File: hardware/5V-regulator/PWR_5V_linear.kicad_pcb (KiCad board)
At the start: 2 copper layers, 19.7 x 19.7 mm, 16 parts, among them P1002 CONN_1, P901 CONN_1, P902 CONN_1, Q1001 MOS_PRO, U1001 LM317M

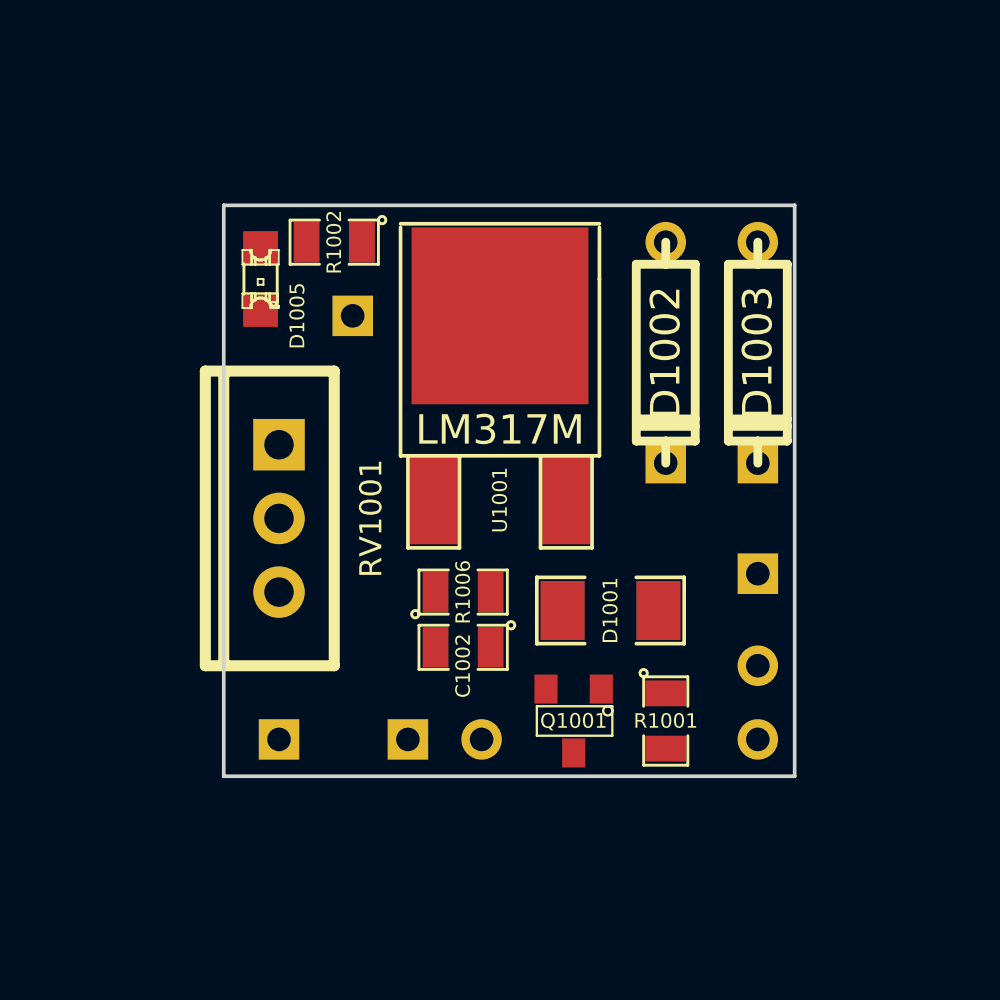
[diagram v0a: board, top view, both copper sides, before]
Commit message: 
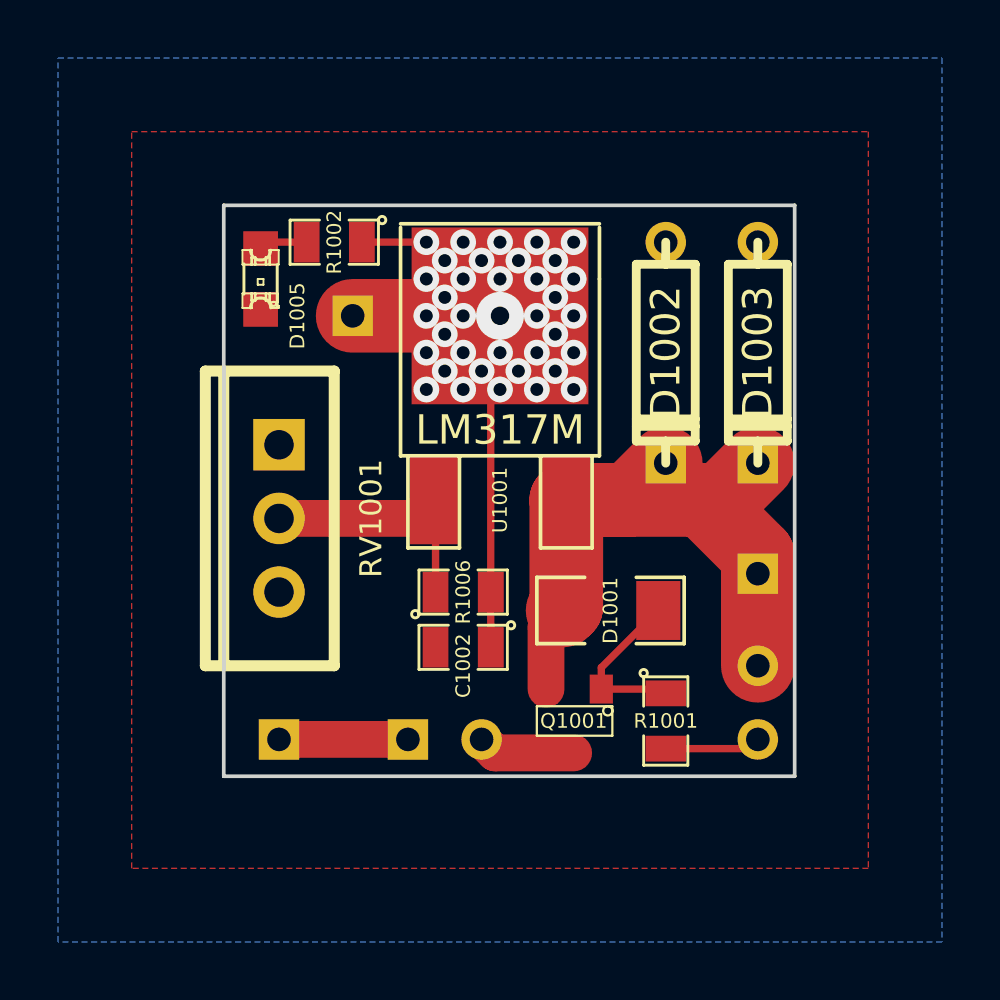
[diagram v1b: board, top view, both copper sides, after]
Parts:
- turned C1001 to 270 degrees
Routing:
- net /5V-REG: track 0.00 -> 62.4 mm, vias 0 -> 37
- net /VBAT: track 0.00 -> 24.4 mm
- net N-000003: track 0.00 -> 8.80 mm
- net N-000007: track 0.00 -> 5.81 mm
- net /Vin: track 0.00 -> 4.44 mm
- net /Vf: track 0.00 -> 3.37 mm
- net GND: track 0.00 -> 3.31 mm
- net N-000005: track 0.00 -> 1.68 mm
- added copper zone on B.Cu, net GND
- added copper zone on F.Cu, net GND
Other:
- net class .05 added: clearance 0.254, trace_width 1.27, via_dia 0.889, via_drill 0.635
- net class .1 added: clearance 0.254, trace_width 2.54, via_dia 1.651, via_drill 1.397

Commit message: 
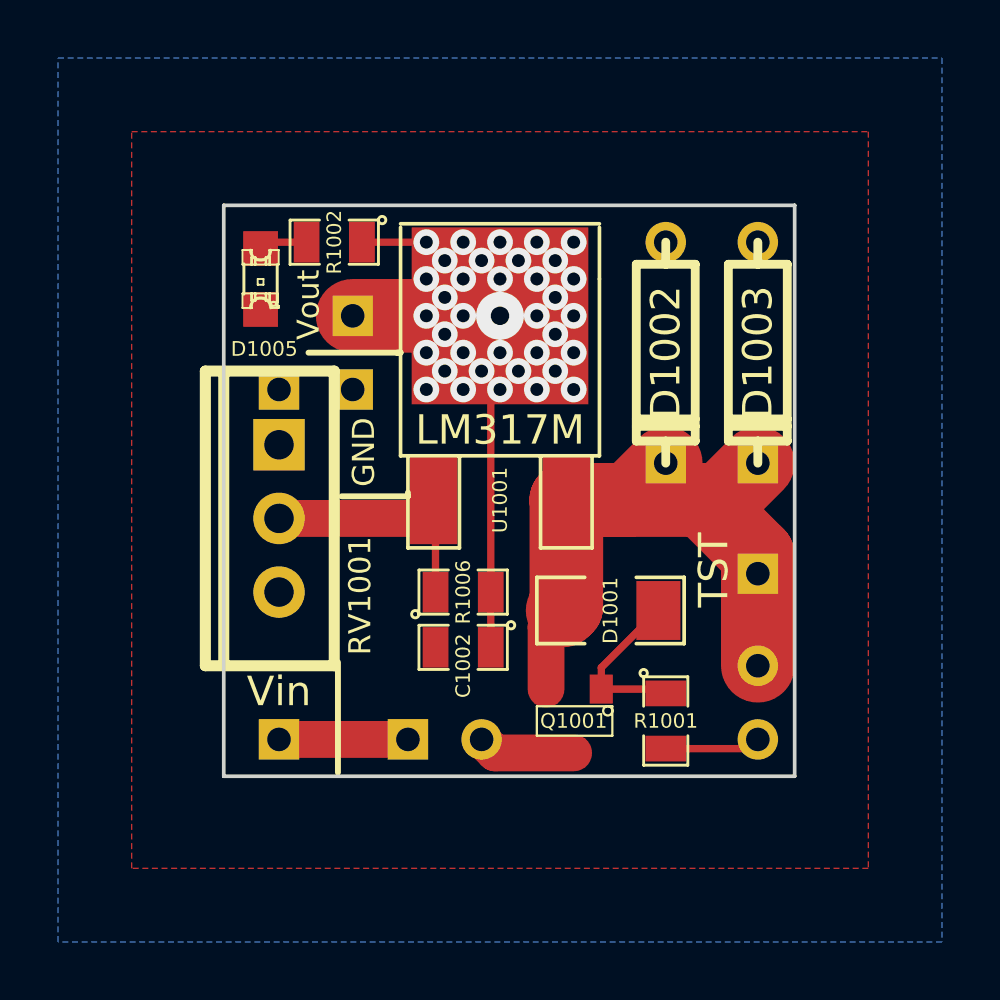
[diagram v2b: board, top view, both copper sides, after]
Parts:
- added P1003: CONN_1, SIL-1, B.Cu at (91.4, 74.9)
- added P1004: CONN_1, SIL-1, B.Cu at (88.9, 74.9)
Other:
- board text added: ".5A FUSE"
- board text added: "ADJ V-REG 1.2V TO 5V"
- board text added: "DAECU for rusEFI R0.01"
- board text added: "GND"
- board text added: "TST"
- board text added: "Vin"
- board text added: "Vout"
